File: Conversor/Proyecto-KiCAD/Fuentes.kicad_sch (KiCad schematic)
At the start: 12 parts

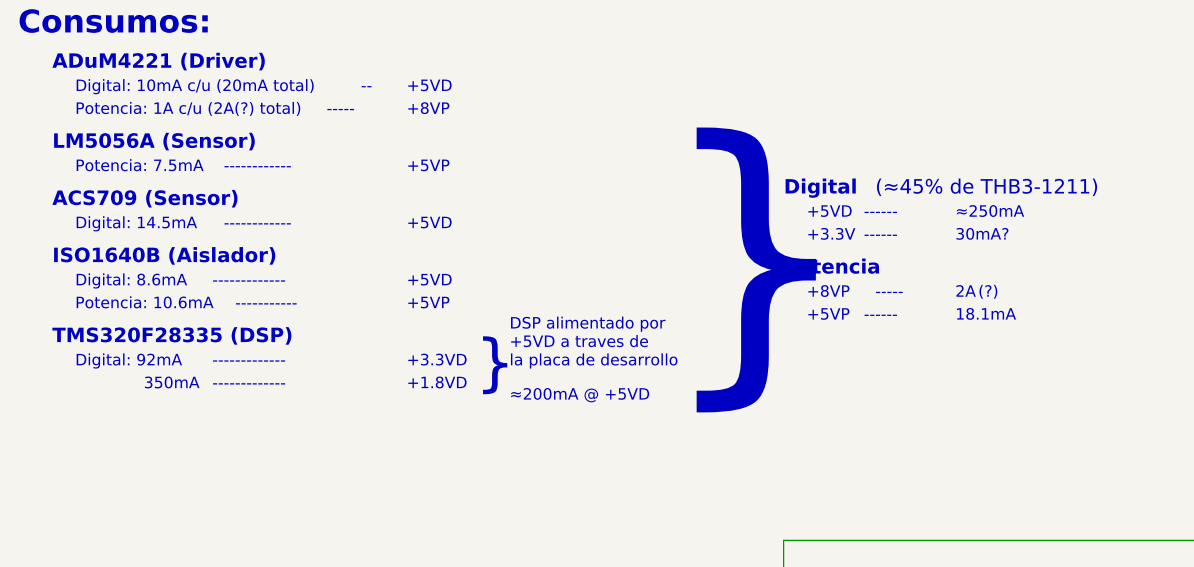
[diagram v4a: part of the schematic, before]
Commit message: Reemplazar ISO1641 por aislador SI8642 (en stock)
- Agregar su datasheet y incluirlo en la lista de componentes
- Conectar tambien la linea de recepcion de datos del LM5056A
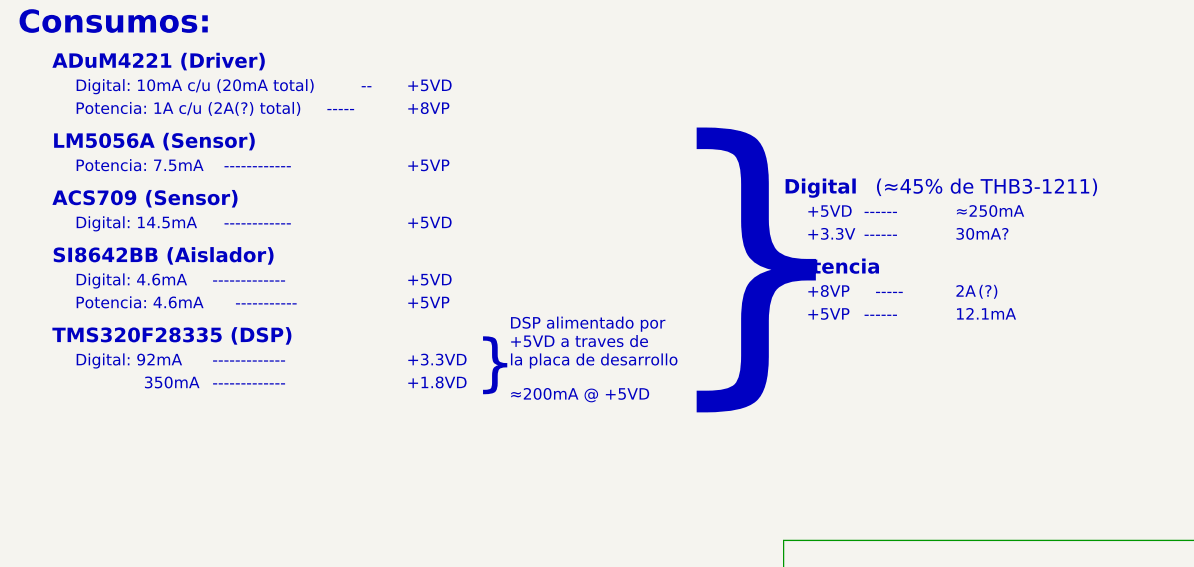
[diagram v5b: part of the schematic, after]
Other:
- note added: "12.1mA"
- note added: "Digital: 4.6mA"
- note added: "Potencia: 4.6mA"
- note added: "SI8642BB (Aislador)"
- note removed: "18.1mA"
- note removed: "Digital: 8.6mA"
- note removed: "ISO1640B (Aislador)"
- note removed: "Potencia: 10.6mA"
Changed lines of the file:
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@@
     (effects (font (size 1.27 1.27)) (justify left bottom))
   )
-  (text "ISO1640B (Aislador)" (at 16.51 41.91 0)
+  (text "SI8642BB (Aislador)" (at 16.51 41.91 0)
     (effects (font (size 1.6 1.6) (thickness 0.32) bold) (justify left bottom))
   )
@@
     (effects (font (size 1.6 1.6) (thickness 0.32) bold) (justify left bottom))
   )
-  (text "Potencia: 10.6mA" (at 19.05 46.99 0)
+  (text "Potencia: 4.6mA" (at 19.05 46.99 0)
     (effects (font (size 1.27 1.27)) (justify left bottom))
   )
@@
     (effects (font (size 1.27 1.27)) (justify left bottom))
   )
-  (text "18.1mA" (at 116.84 48.26 0)
+  (text "12.1mA" (at 116.84 48.26 0)
     (effects (font (size 1.27 1.27)) (justify left bottom))
   )
@@
     (effects (font (size 1.27 1.27)) (justify left bottom))
   )
-  (text "Digital: 8.6mA" (at 19.05 44.45 0)
+  (text "Digital: 4.6mA" (at 19.05 44.45 0)
     (effects (font (size 1.27 1.27)) (justify left bottom))
   )

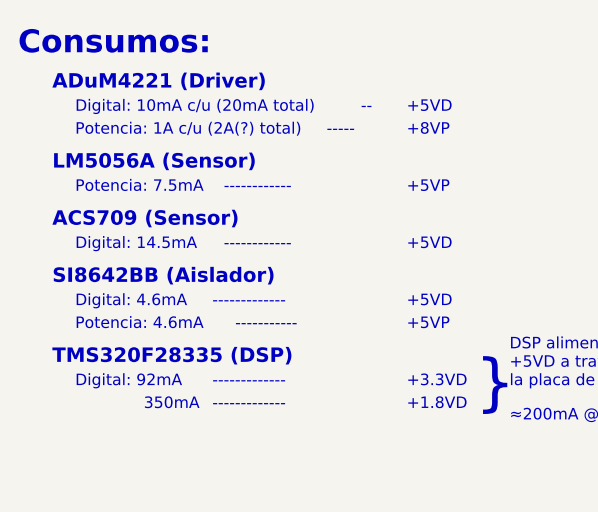
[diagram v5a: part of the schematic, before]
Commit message: Seleccion definitiva de drivers y sensores (ya comprados)
- Driver Infineon 2ED21834-S06J: Con DT y sin asilamiento
  - Optoacopladores ACPL-P480 para aislarlos
  - Falta implementarlos (drivers y optos) en el esquematico
- LM5056 como sensor de corriente de entrada y tension de entrada/salida
- Sensor de efecto hall TMCS1100A4 para corriente de salida
  - Ya esta agregado al esquematico (reemplazo ACS709)
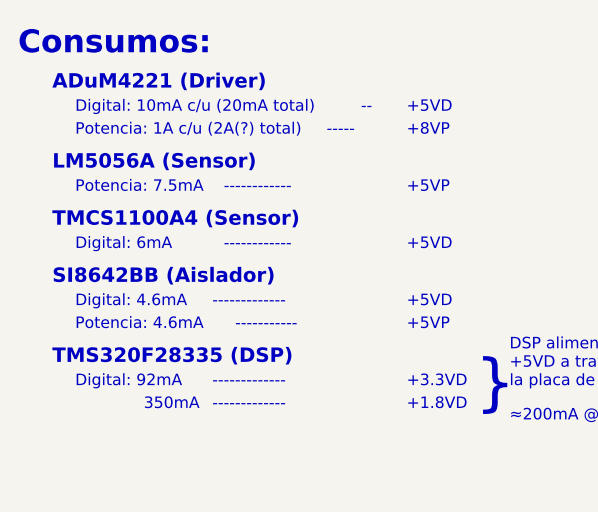
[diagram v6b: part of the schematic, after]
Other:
- note added: "Digital: 6mA"
- note added: "TMCS1100A4 (Sensor)"
- note removed: "ACS709 (Sensor)"
- note removed: "Digital: 14.5mA"
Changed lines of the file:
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@@
     (effects (font (size 1.27 1.27)) (justify left bottom))
   )
-  (text "ACS709 (Sensor)" (at 16.51 35.56 0)
+  (text "TMCS1100A4 (Sensor)" (at 16.51 35.56 0)
     (effects (font (size 1.6 1.6) (thickness 0.32) bold) (justify left bottom))
   )
@@
     (effects (font (size 1.27 1.27)) (justify left bottom))
   )
-  (text "Digital: 14.5mA" (at 19.05 38.1 0)
+  (text "Digital: 6mA" (at 19.05 38.1 0)
     (effects (font (size 1.27 1.27)) (justify left bottom))
   )

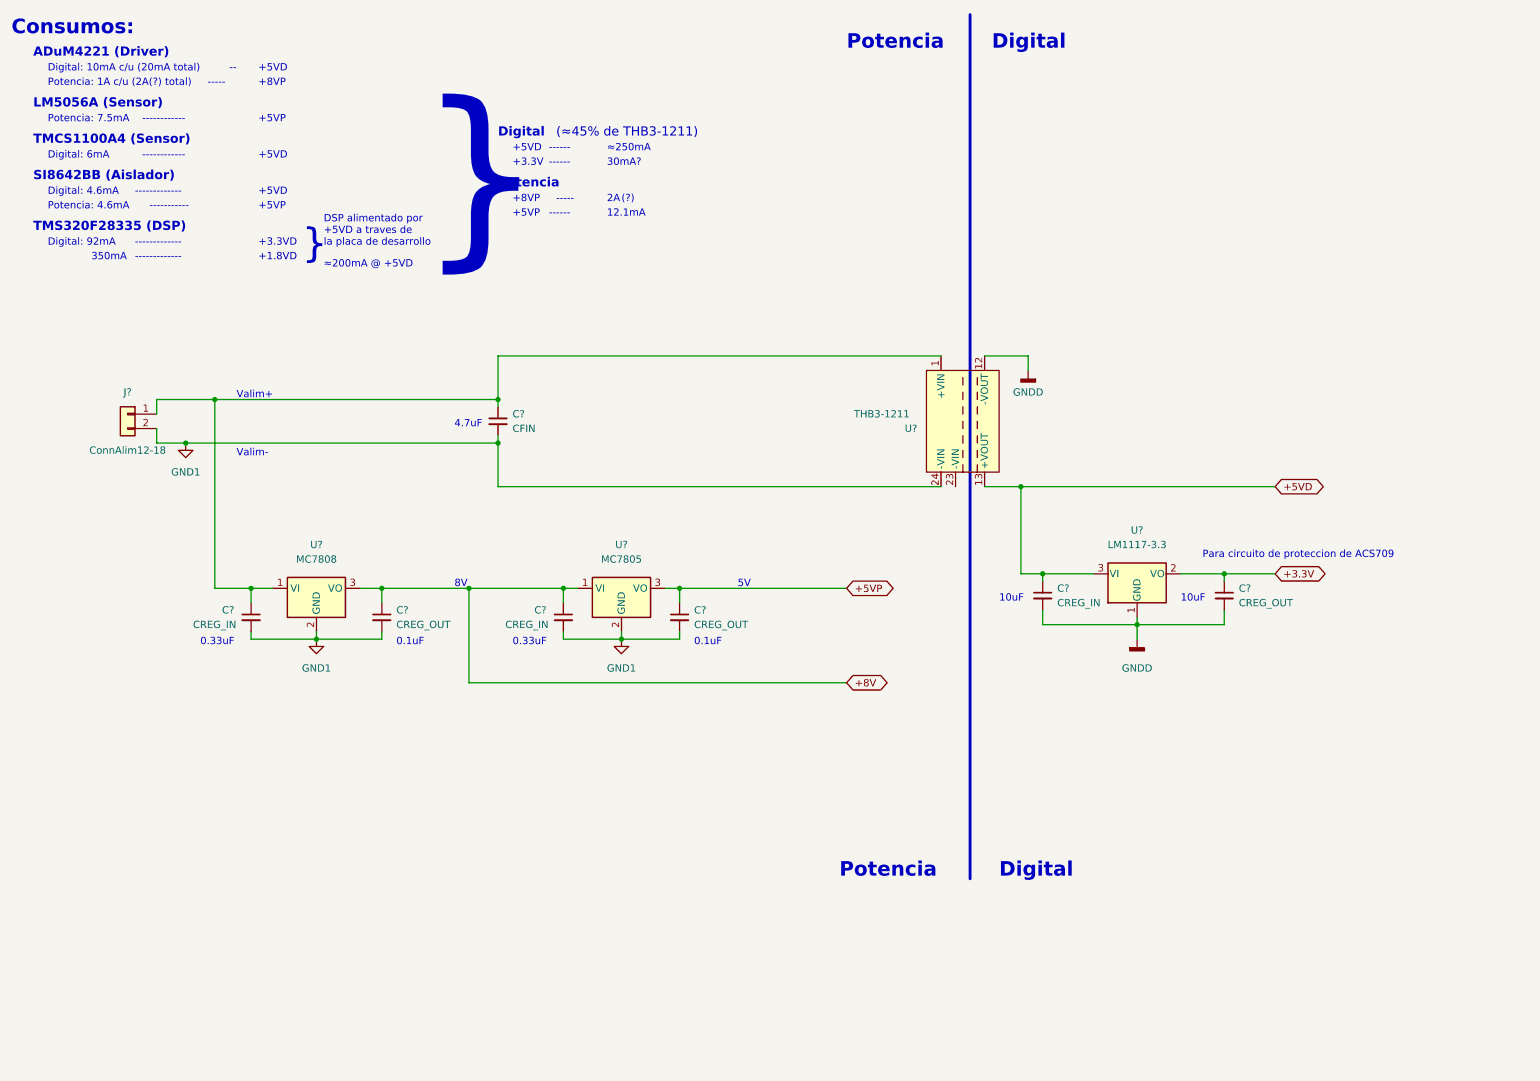
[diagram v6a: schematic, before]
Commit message: Reemplazar drivers aislados por driver+optos
- Solo faltaria ver la alimentacion de +15V para los dos drivers
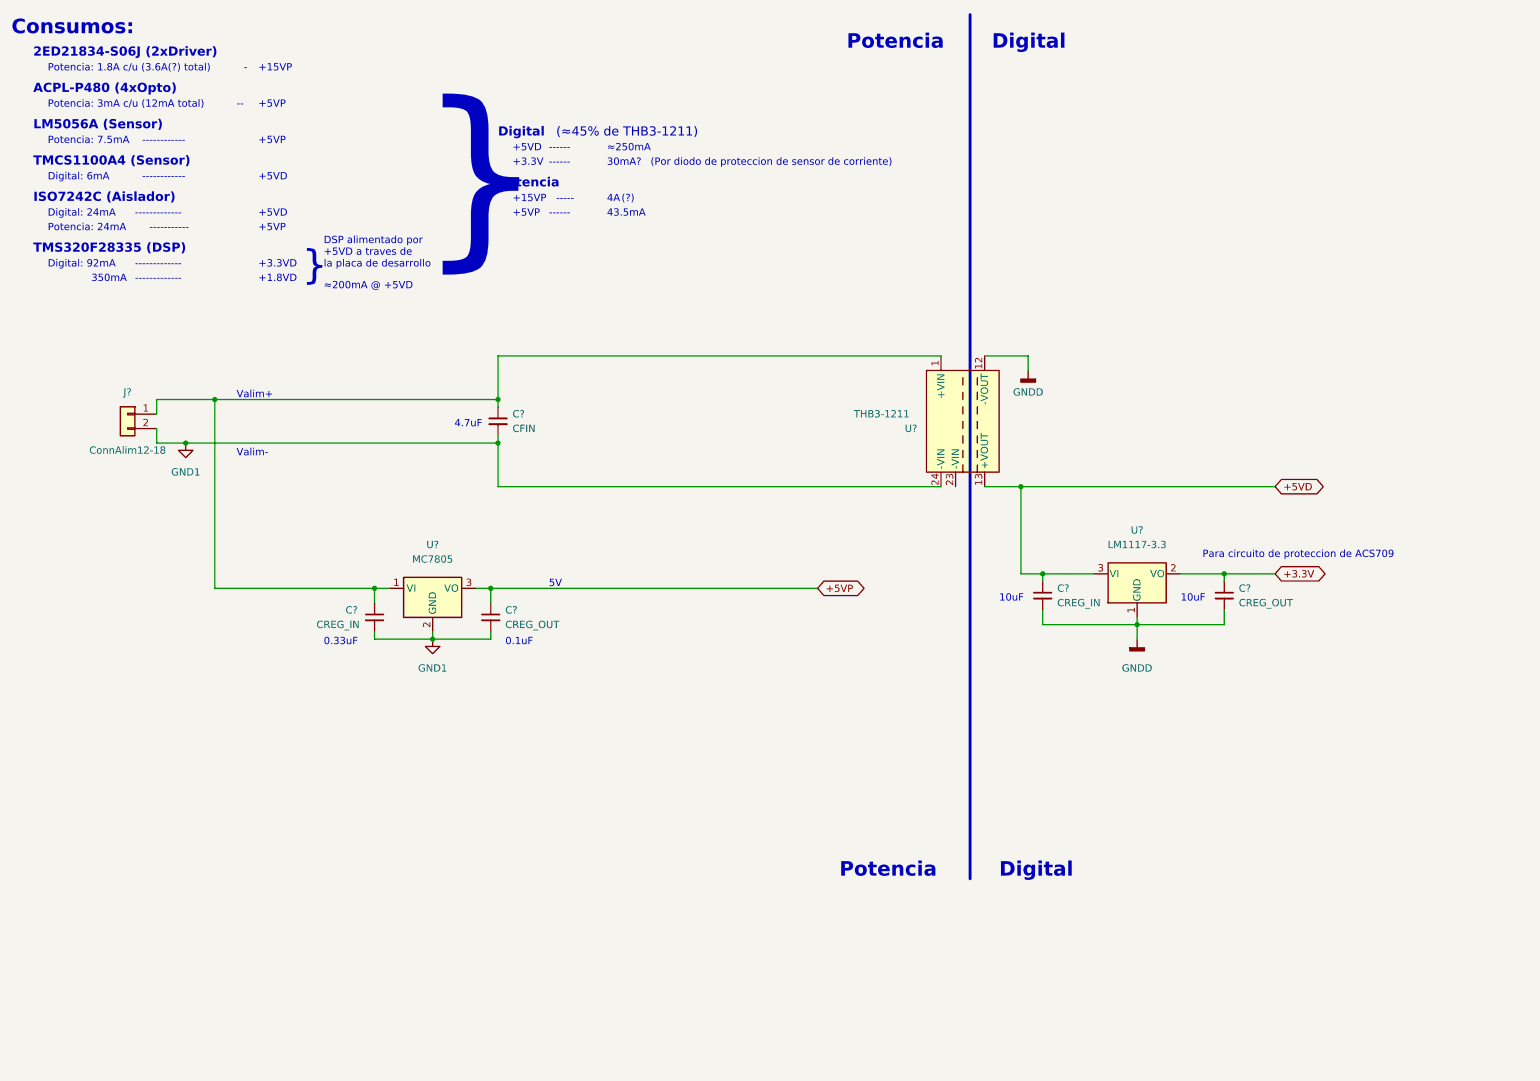
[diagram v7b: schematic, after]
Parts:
- removed C?: CREG_OUT, symbol Device:C_Small
- removed C?: CREG_IN, symbol Device:C_Small
- removed U?: MC7808, symbol Componentes proyecto:MC7808
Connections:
- net +8V is gone; now on an unnamed net: C?.1, U?.1 (VI)
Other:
- note added: "(Por diodo de proteccion de sensor de corriente)"
- note added: "+15VP"
- note added: "-"
- note added: "2ED21834-S06J (2xDriver)"
- note added: "43.5mA"
- note added: "4A"
- note added: "ACPL-P480 (4xOpto)"
- note added: "Digital: 24mA"
- note added: "ISO7242C (Aislador)"
- note added: "Potencia: 1.8A c/u (3.6A(?) total)"
- note added: "Potencia: 24mA"
- note added: "Potencia: 3mA c/u (12mA total)"
- note removed: "+8VP"
- note removed: "12.1mA"
- note removed: "2A"
- note removed: "8V"
- note removed: "ADuM4221 (Driver)"
- note removed: "Digital: 10mA c/u (20mA total)"
- note removed: "Digital: 4.6mA"
- note removed: "Potencia: 1A c/u (2A(?) total)"
- note removed: "Potencia: 4.6mA"
- note removed: "SI8642BB (Aislador)"
- moved on the sheet: C?, U?

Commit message: Agregar alimentacion de 10V para los drivers
- Usar LM2576T-ADJ para obtener salida de 10V con 3A de Iout_max (1.1A
por driver se necesitan)
  - Preguntar si esta bien, porque requiere un inductor de 100uH, si no
usar alimentacion externa de 24V y un regulador normal de 15V
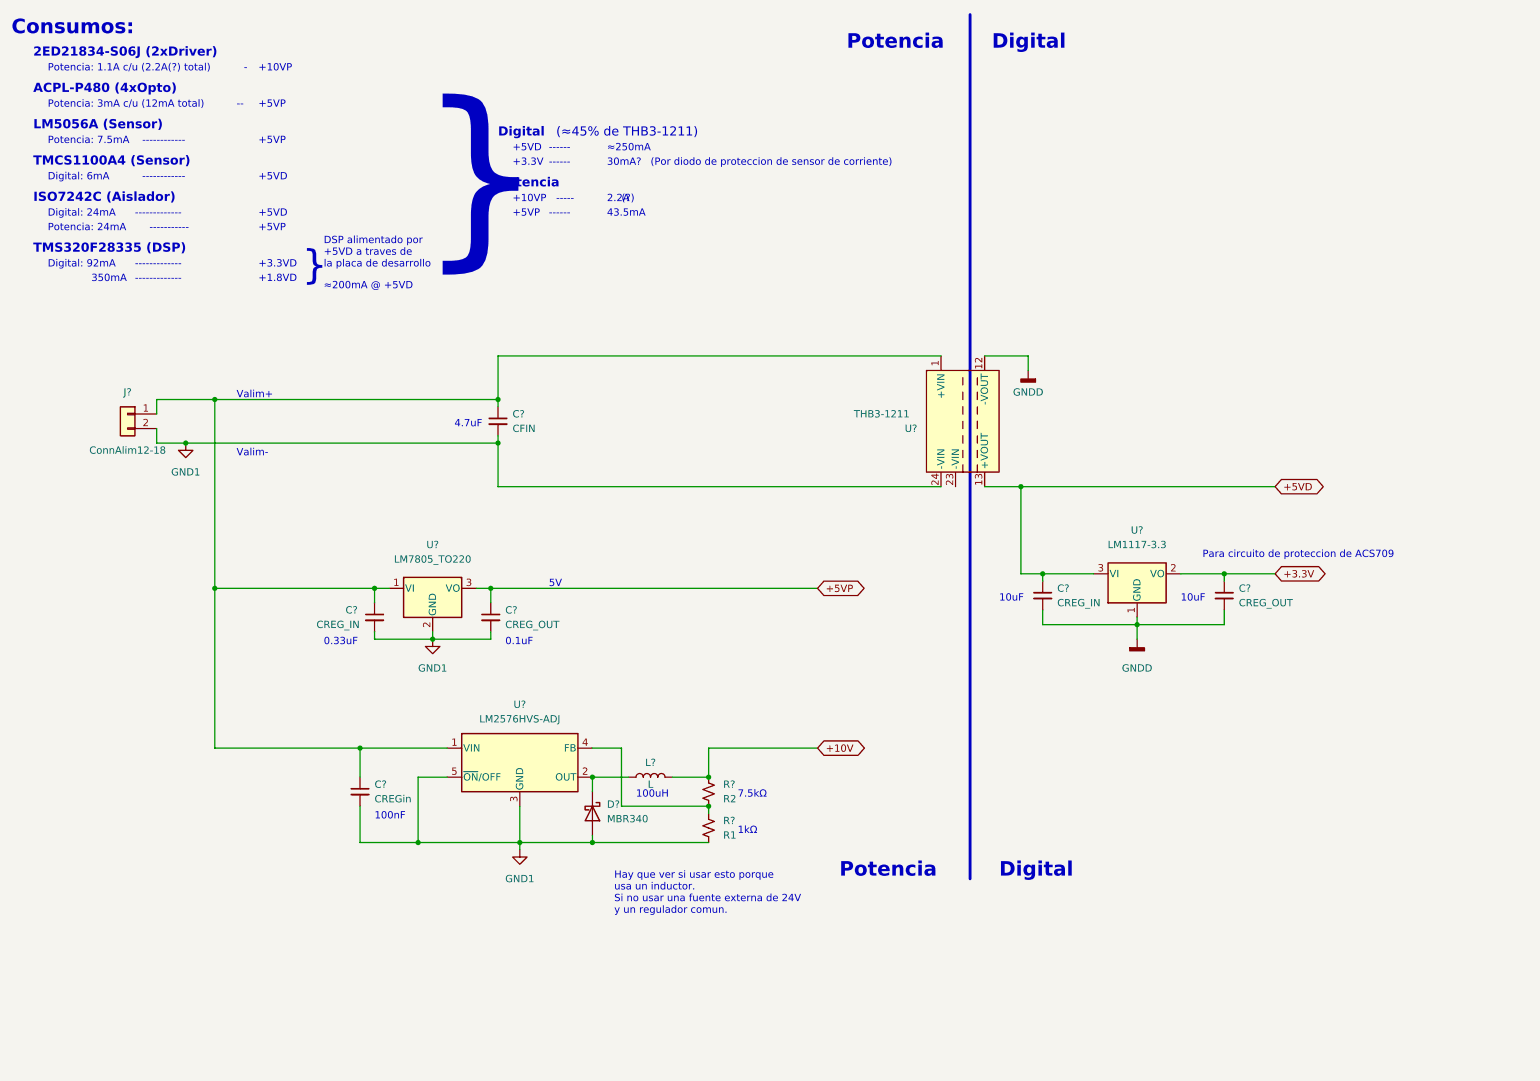
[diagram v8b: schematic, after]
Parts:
- removed U?: MC7805, symbol Componentes proyecto:MC7805
- added C?: CREGin, symbol Device:C_Small
- added D?: MBR340, Diode_THT:D_DO-201AD_P15.24mm_Horizontal, symbol Diode:MBR340
- added L?: L, symbol Device:L
- added R?: R2, symbol Device:R_Small_US
- added R?: R1, symbol Device:R_Small_US
- added U?: LM7805_TO220, Package_TO_SOT_THT:TO-220-3_Vertical, symbol Regulator_Linear:LM7805_TO220
- added U?: LM2576HVS-ADJ, Package_TO_SOT_SMD:TO-263-5_TabPin3, symbol Regulator_Switching:LM2576HVS-ADJ
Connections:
- net +5VP: now also U?.3 (VO)
- net GND1: now also C?.2, D?.2 (A), R?.2, U?.2 (GND), U?.3 (GND), U?.5 (~{ON}/OFF)
- net at C?.1, C?.1, J?.1 (Pin_1)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: now also C?.1, U?.1 (VI), U?.1 (VIN)
- new net: R?.1, R?.2, U?.4 (FB)
- new net: D?.1 (K), L?.1, U?.2 (OUT)
- new net +10V: L?.2, R?.1
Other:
- note added: "+10VP"
- note added: "100nF"
- note added: "100uH"
- note added: "1kΩ"
- note added: "2.2A"
- note added: "7.5kΩ"
- note added: "Hay que ver si usar esto porque usa un inductor. Si no usar una fuente externa de 24V y un regulador comun."
- note added: "Potencia: 1.1A c/u (2.2A(?) total)"
- note removed: "+15VP"
- note removed: "4A"
- note removed: "Potencia: 1.8A c/u (3.6A(?) total)"
